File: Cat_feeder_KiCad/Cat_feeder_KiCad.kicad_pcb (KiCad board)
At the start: 2 copper layers, 17 parts, among them J1 Conn_01x03_Pin, J2 Conn_01x04_Pin, J3 Conn_01x04_Pin, SW1 SW_Push, SW2 Reset button, U1 ESP32-S3-WROOM-1, U3 ER_OLEDM0.91_1x-I2C, U4 LD1117V33, U5 DS3231M

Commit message: some schematic work + kicad crashed
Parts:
- removed C5: 100nF, Capacitor_SMD:C_0805_2012Metric
- removed D1: 1N4148, Diode_THT:D_DO-35_SOD27_P7.62mm_Horizontal
- removed J3: Conn_01x04_Pin, Connector_PinHeader_2.54mm:PinHeader_1x04_P2.54mm_Horizontal
- removed R1: 100V, Resistor_SMD:R_0805_2012Metric
- removed U3: ER_OLEDM0.91_1x-I2C, Display:ER_OLEDM0.91_1x-I2C
- added BT2: Battery_Cell, Battery:BatteryHolder_Keystone_3034_1x20mm, F.Cu at (102.5, 98.0)
- added C7: 100nF, Capacitor_SMD:C_0805_2012Metric, F.Cu at (176.6, 85.0)
- added C8: 1uF, Capacitor_SMD:C_0805_2012Metric, F.Cu at (158.1, 61.5)
- added D2: 1N4148, Diode_THT:D_DO-35_SOD27_P7.62mm_Horizontal, F.Cu at (164.2, 95.0)
- added R5: 100Ω, Resistor_SMD:R_0805_2012Metric, F.Cu at (167.6, 102.5)
- added R7: 4.7K, Resistor_SMD:R_0805_2012Metric, F.Cu at (124.5, 86.0)
- added R8: 4.7K, Resistor_SMD:R_0805_2012Metric, F.Cu at (116.9, 86.0)
- added Y1: Crystal, Crystal:Crystal_SMD_0603-2Pin_6.0x3.5mm, F.Cu at (146.5, 85.0)
- U5: value DS3231M -> PCF85263AT; footprint Package_SO:SOIC-16W_7.5x10.3mm_P1.27mm -> Package_SO:SOIC-8_3.9x4.9mm_P1.27mm
- moved R4 104.3 mm to (97.5, 64.0)
- moved SW1 75.1 mm to (104.0, 61.5)
- moved SW2 73.8 mm to (103.8, 73.2)
- moved U5 71.8 mm to (147.0, 74.1)
- moved U1 69.4 mm to (125.2, 64.2)
- moved U4 58.8 mm to (144.5, 63.0)
- moved J1 47.6 mm to (167.5, 61.5)
- moved C1 36.8 mm to (176.6, 61.0)
- moved C2 33.9 mm to (176.6, 67.0)
- moved C3 31.1 mm to (176.6, 73.0), turned to 180 degrees
- moved C4 28.2 mm to (176.6, 79.0)
- moved J2 25.2 mm to (167.5, 76.2)
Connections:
- J2 pad 3: /SDA -> /SCL
- J2 pad 4: /SCL -> /SDA
- U1 pad 11: /SCL_IO18 -> /SDA
- U1 pad 18: /RTC_board/SCL -> unconnected-(U1-IO10-Pad18)
- U1 pad 19: /RTC_board/SDA -> unconnected-(U1-IO11-Pad19)
- U1 pad 23: /SDA_IO21 -> /SCL
- U1 pad 27: unconnected-(U1-IO0-Pad27) -> /SDA_IO
- U1 pad 39: unconnected-(U1-IO1-Pad39) -> /SCL_I0
- U1 pad 6: unconnected-(U1-IO6-Pad6) -> /INTA_IO6
- U5 pad 1: unconnected-(U5-32KHZ-Pad1) -> Net-(U5-OSCI)
- U5 pad 2: +3.3V -> Net-(U5-OSCO)
- U5 pad 3: unconnected-(U5-~{INT}/SQW-Pad3) -> Net-(D2-K)
- U5 pad 4: unconnected-(U5-~{RST}-Pad4) -> GND
- U5 pad 5: GND -> /SDA_IO
- U5 pad 6: GND -> /SCL_I0
- U5 pad 7: GND -> /INTA_IO6
- U5 pad 8: GND -> +3.3V
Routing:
- net GND: track 0.00 -> 217.4 mm, vias 0 -> 1
- net +3.3V: track 0.00 -> 190.6 mm, vias 0 -> 2
- net Net-(BT2-+): track 0.00 -> 94.5 mm
- net /INTA_IO6: track 0.00 -> 61.6 mm, vias 0 -> 2
- net /SDA: track 0.00 -> 61.4 mm, vias 0 -> 1
- net /SCL: track 0.00 -> 56.8 mm, vias 0 -> 1
- net Net-(J1-Pin_3): track 0.00 -> 52.7 mm, vias 0 -> 3
- net Net-(U1-IO13): track 0.00 -> 45.5 mm, vias 0 -> 2
- net Net-(D2-K): track 0.00 -> 45.0 mm
- net /SDA_IO: track 0.00 -> 37.7 mm, vias 0 -> 2
- net +5V: track 0.00 -> 33.7 mm
- net /SCL_I0: track 0.00 -> 28.9 mm, vias 0 -> 2
- net Net-(U5-OSCI): track 0.00 -> 15.2 mm, vias 0 -> 2
- net Net-(U5-OSCO): track 0.00 -> 13.4 mm, vias 0 -> 2
- net Net-(D2-A): track 0.00 -> 10.5 mm

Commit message: finished pcb
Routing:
- added copper zone on F.Cu, net GND
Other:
- board outline added: 102.8 x 51.6 mm

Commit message: done for the day
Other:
- board size 102.8 x 51.6 mm -> 98.8 x 51.6 mm
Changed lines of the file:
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@@
 			(outputformat 1)
 			(mirror no)
-			(drillshape 1)
+			(drillshape 0)
 			(scaleselection 1)
-			(outputdirectory "")
+			(outputdirectory "../../Cat_feeder_GERBERS/")
 		)
 	)
@@
 	(gr_line
 		(start 144.539757 109.209218)
-		(end 182.600457 109.126588)
+		(end 178 109.126588)
 		(stroke
 			(width 0)
@@
 	)
 	(gr_line
-		(start 182.284945 57.696953)
-		(end 144.525929 57.637235)
+		(start 178 109.126588)
+		(end 179.86254 108.443401)
 		(stroke
 			(width 0)
@@
 	)
 	(gr_line
-		(start 182.600457 109.126588)
-		(end 183.86254 108.443401)
+		(start 178.284945 57.696953)
+		(end 144.525929 57.637235)
 		(stroke
 			(width 0)
@@
 	)
 	(gr_line
-		(start 183.906031 58.552016)
-		(end 182.284945 57.696953)
+		(start 179.906031 58.552016)
+		(end 178.284945 57.696953)
 		(stroke
 			(width 0)
@@
 	)
 	(gr_arc
-		(start 183.906031 58.552016)
-		(mid 184.263468 58.753636)
-		(end 184.608972 58.975083)
+		(start 179.906031 58.552016)
+		(mid 180.263468 58.753636)
+		(end 180.608972 58.975083)
 		(stroke
 			(width 0)
@@
 	)
 	(gr_arc
-		(start 185.005412 107.683678)
-		(mid 184.45118 108.08942)
-		(end 183.86254 108.443401)
+		(start 181.005412 107.683678)
+		(mid 180.45118 108.08942)
+		(end 179.86254 108.443401)
 		(stroke
 			(width 0)
@@
 	)
 	(gr_line
-		(start 185.3826 59.54338)
-		(end 184.608972 58.975083)
+		(start 181.3826 59.54338)
+		(end 180.608972 58.975083)
 		(stroke
 			(width 0)
@@
 	)
 	(gr_line
-		(start 186.106852 60.158937)
-		(end 185.3826 59.54338)
+		(start 182.106852 60.158937)
+		(end 181.3826 59.54338)
 		(stroke
 			(width 0)
@@
 	)
 	(gr_arc
-		(start 186.106852 60.158937)
-		(mid 186.390252 60.434108)
-		(end 186.656215 60.726166)
+		(start 182.106852 60.158937)
+		(mid 182.390252 60.434108)
+		(end 182.656215 60.726166)
 		(stroke
 			(width 0)
@@
 	)
 	(gr_arc
-		(start 186.190072 106.612843)
-		(mid 185.613218 107.165382)
-		(end 185.005412 107.683678)
+		(start 182.190072 106.612843)
+		(mid 181.613218 107.165382)
+		(end 181.005412 107.683678)
 		(stroke
 			(width 0)
@@
 	)
 	(gr_arc
-		(start 186.656215 60.726166)
-		(mid 187.3795 61.730978)
-		(end 187.924514 62.842622)
+		(start 182.656215 60.726166)
+		(mid 183.3795 61.730978)
+		(end 183.924514 62.842622)
 		(stroke
 			(width 0)
@@
 	)
 	(gr_arc
-		(start 187.248511 105.407005)
-		(mid 186.736671 106.025179)
-		(end 186.190072 106.612843)
+		(start 183.248511 105.407005)
+		(mid 182.736671 106.025179)
+		(end 182.190072 106.612843)
 		(stroke
 			(width 0)
@@
 	)
 	(gr_arc
-		(start 187.924514 62.842622)
-		(mid 188.311791 64.092346)
-		(end 188.517541 65.384421)
+		(start 183.924514 62.842622)
+		(mid 184.311791 64.092346)
+		(end 184.517541 65.384421)
 		(stroke
 			(width 0)
@@
 	)
 	(gr_arc
-		(start 188.008403 104.236037)
-		(mid 187.653977 104.838082)
-		(end 187.248511 105.407005)
+		(start 184.008403 104.236037)
+		(mid 183.653977 104.838082)
+		(end 183.248511 105.407005)
 		(stroke
 			(width 0)
@@
 	)
 	(gr_arc
-		(start 188.362715 103.044744)
-		(mid 188.245142 103.65811)
-		(end 188.008403 104.236037)
+		(start 184.362715 103.044744)
+		(mid 184.245142 103.65811)
+		(end 184.008403 104.236037)
 		(stroke
 			(width 0)
@@
 	)
 	(gr_line
-		(start 188.362715 103.044744)
-		(end 188.521423 100.470324)
+		(start 184.362715 103.044744)
+		(end 184.521423 100.470324)
 		(stroke
 			(width 0)
@@
 	)
 	(gr_line
-		(start 188.521423 100.470324)
-		(end 188.61549 95.821186)
+		(start 184.521423 100.470324)
+		(end 184.61549 95.821186)
 		(stroke
 			(width 0)
@@
 	)
 	(gr_line
-		(start 188.61549 95.821186)
-		(end 188.683715 84.073976)
+		(start 184.61549 95.821186)
+		(end 184.683715 84.073976)
 		(stroke
 			(width 0)
@@
 	)
 	(gr_line
-		(start 188.683715 84.073976)
-		(end 188.715056 69.93125)
+		(start 184.683715 84.073976)
+		(end 184.715056 69.93125)
 		(stroke
 			(width 0)
@@
 	)
 	(gr_line
-		(start 188.715056 69.93125)
-		(end 188.517541 65.384421)
+		(start 184.715056 69.93125)
+		(end 184.517541 65.384421)
 		(stroke
 			(width 0)
@@
 			(pts
 				(xy 91 60) (xy 90.5 60.5) (xy 88.5 66.5) (xy 86.5 90) (xy 87 103) (xy 89.5 106.5) (xy 97 108.5)
-				(xy 107 109) (xy 177.5 108.5) (xy 183 102.5) (xy 182.5 68.5) (xy 180.5 58) (xy 100.5 58)
+				(xy 107 109) (xy 177.5 108.5) (xy 183 102.5) (xy 182.5 68.5) (xy 179.5 58.5) (xy 100.5 58)
 			)
 		)

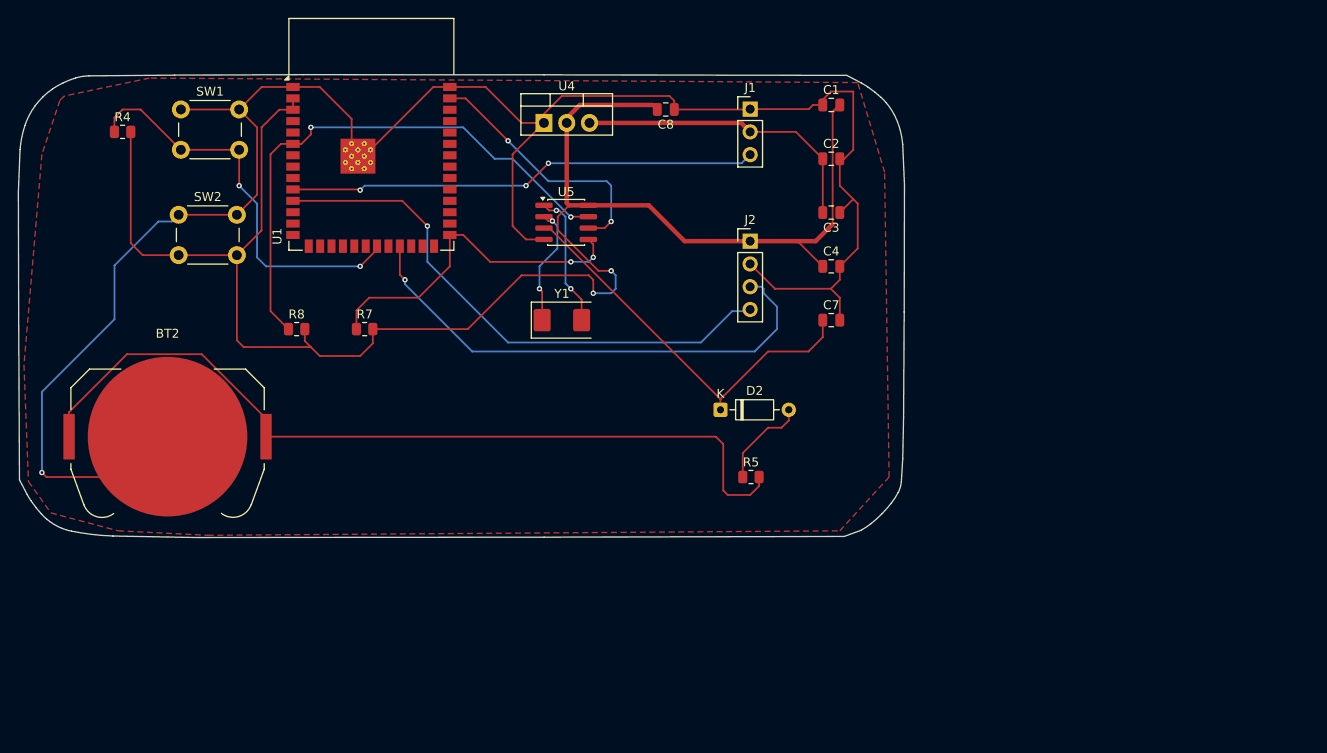
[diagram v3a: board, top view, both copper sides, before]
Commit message: added mounting holes
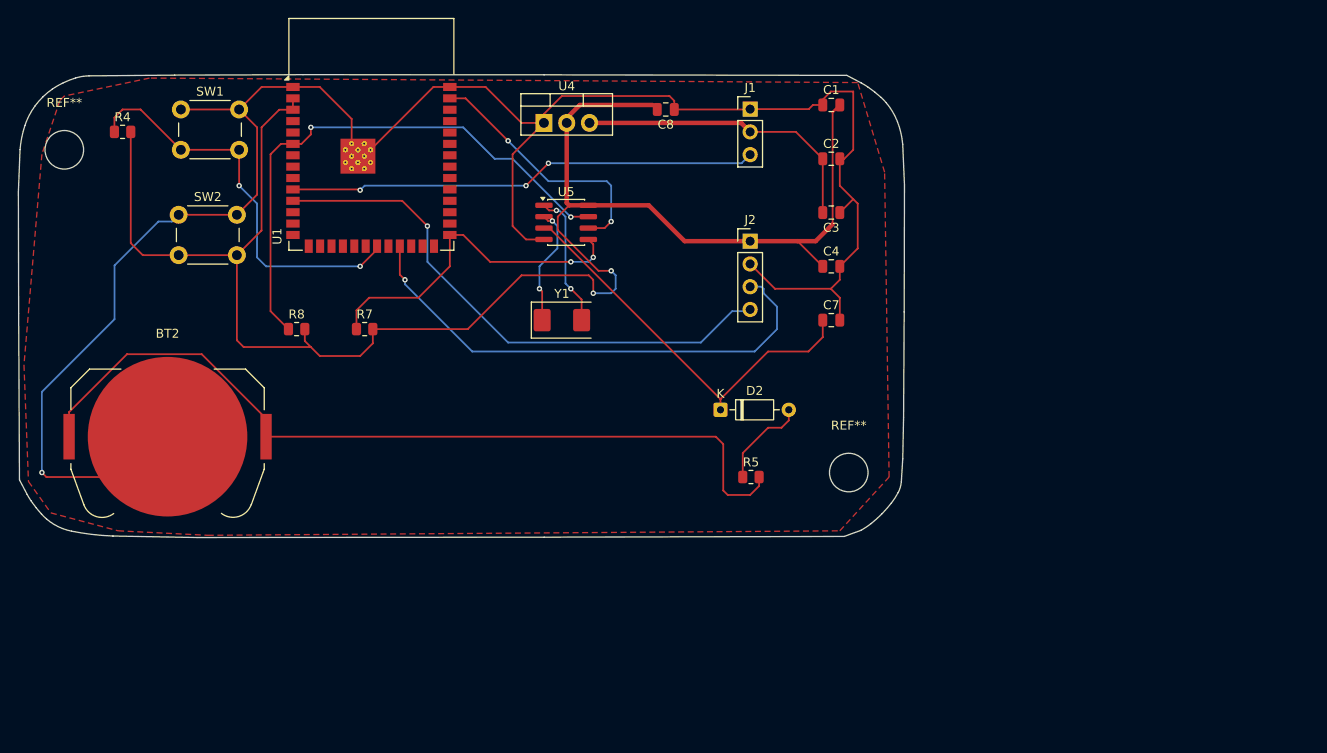
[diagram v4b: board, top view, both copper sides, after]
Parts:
- added REF**: MountingHole_4.3mm_M4, MountingHole:MountingHole_4.3mm_M4, F.Cu at (178.5, 102.0)
- added REF**: MountingHole_4.3mm_M4, MountingHole:MountingHole_4.3mm_M4, F.Cu at (91.0, 66.0)

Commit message: updated cuz i forgot my power source
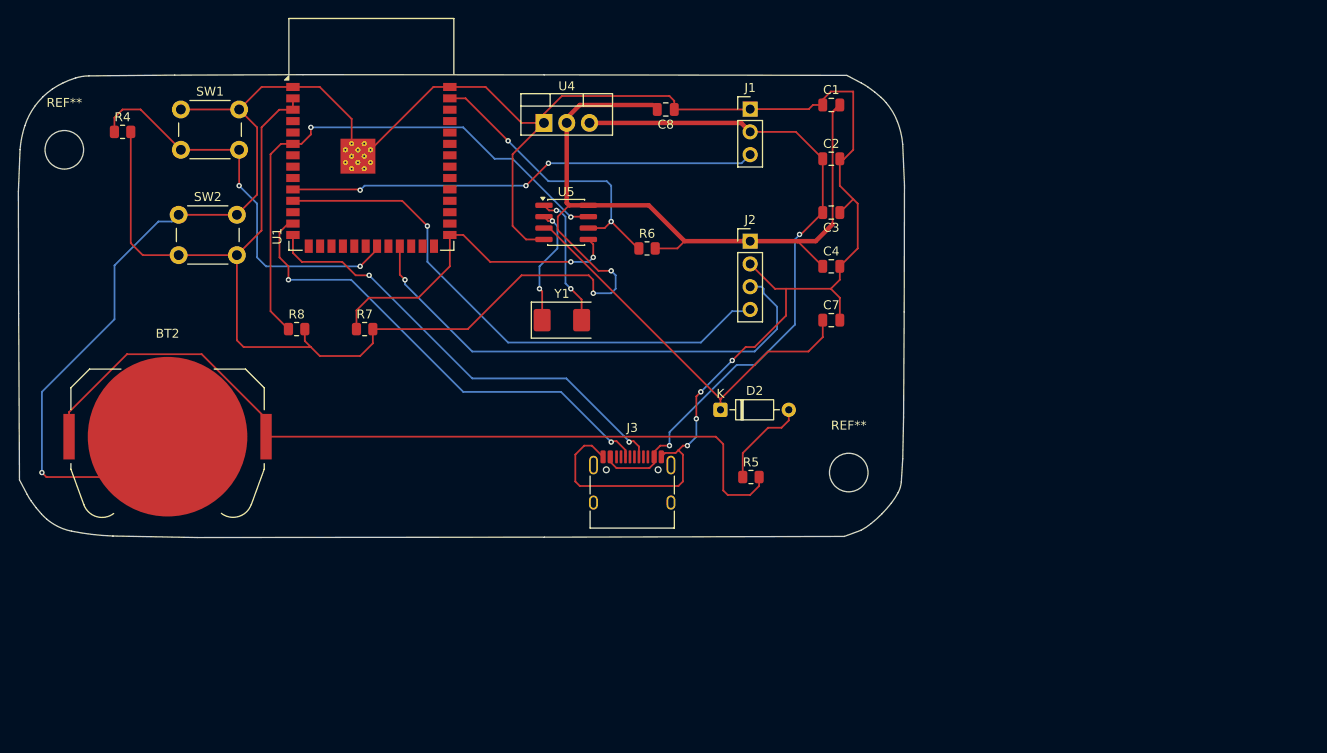
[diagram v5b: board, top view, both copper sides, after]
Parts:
- added J3: USB_C_Receptacle_USB2.0_14P, Connector_USB:USB_C_Receptacle_HRO_TYPE-C-31-M-12, F.Cu at (154.3, 104.3)
- added R6: 4.7K, Resistor_SMD:R_0805_2012Metric, F.Cu at (156.0, 77.0)
- J1: value Conn_01x03_Pin -> Servo motor connector
- J2: value Conn_01x04_Pin -> OLED connector
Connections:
- U1 pad 13: unconnected-(U1-USB_D--Pad13) -> Net-(U1-USB_D-)
- U1 pad 14: unconnected-(U1-USB_D+-Pad14) -> Net-(U1-USB_D+)
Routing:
- net Net-(U1-USB_D-): track 0.00 -> 54.0 mm, vias 0 -> 2
- net Net-(U1-USB_D+): track 0.00 -> 50.9 mm, vias 0 -> 2
- net GND: track 217.2 -> 266.4 mm, vias 1 -> 5
- net +5V: track 33.7 -> 77.3 mm, vias 0 -> 2
- net /SCL_I0: track 28.9 -> 33.2 mm
- net +3.3V: track 190.6 -> 194.2 mm
- removed copper zone on F.Cu, net GND

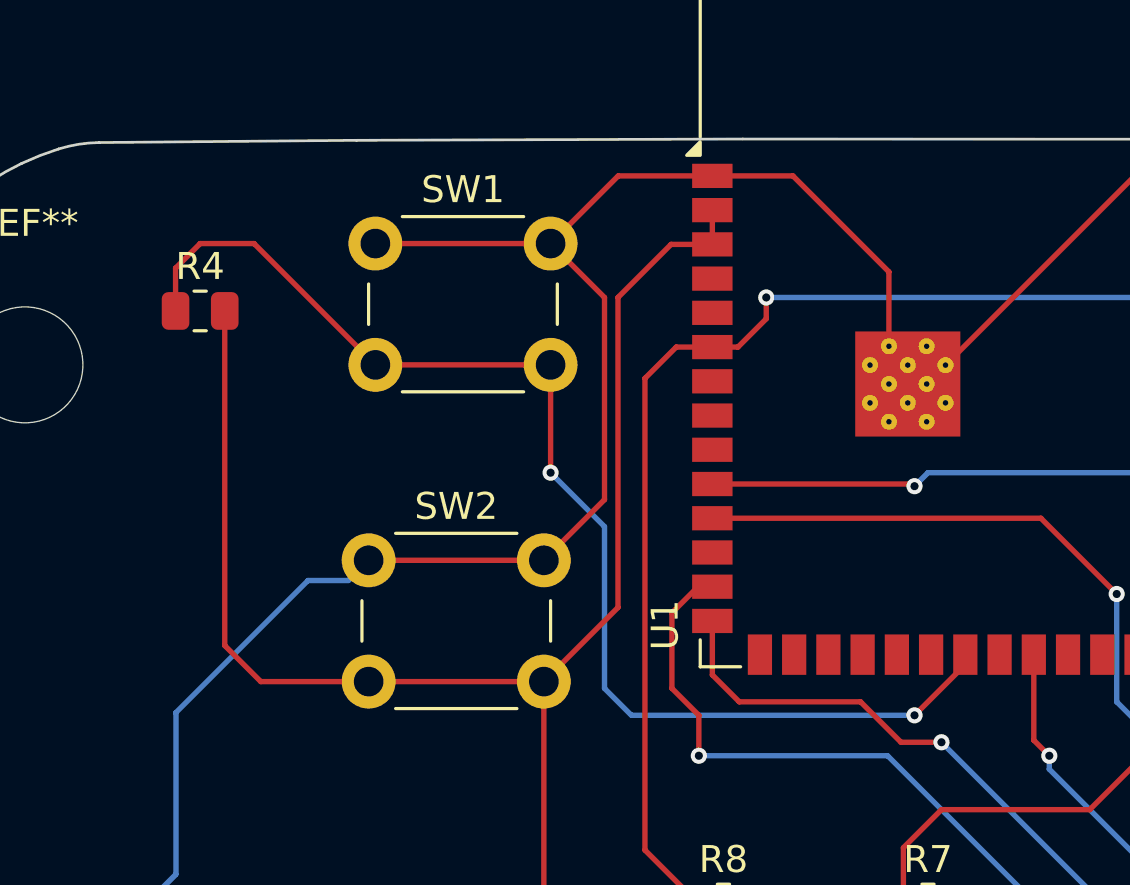
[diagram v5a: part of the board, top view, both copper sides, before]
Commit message: deleted a button
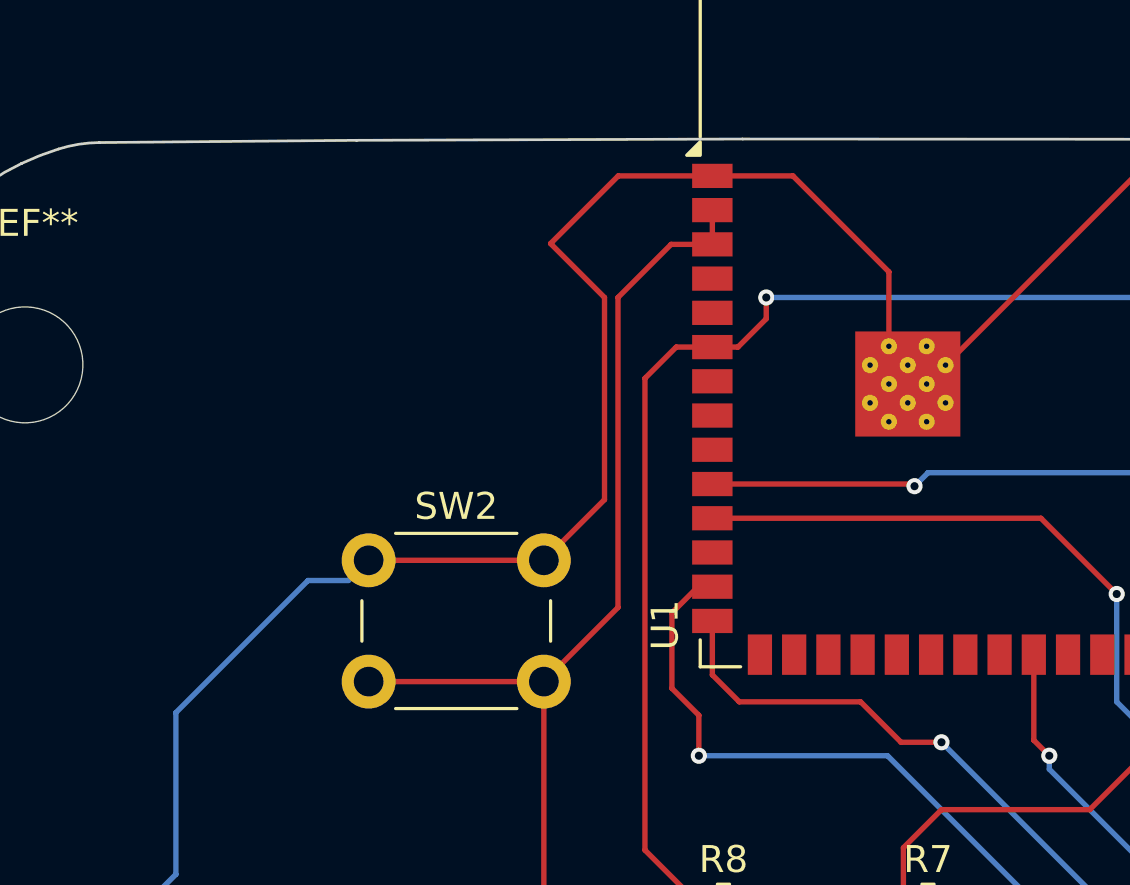
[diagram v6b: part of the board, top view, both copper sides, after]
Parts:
- removed R4: 10K, Resistor_SMD:R_0805_2012Metric
- removed SW1: SW_Push, Button_Switch_THT:SW_PUSH_6mm
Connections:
- U1 pad 21: Net-(U1-IO13) -> unconnected-(U1-IO13-Pad21)
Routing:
- net Net-(U1-IO13): track 45.5 -> 0.00 mm, vias 2 -> 0
- net +3.3V: track 194.2 -> 175.9 mm
- net GND: track 266.4 -> 259.9 mm
